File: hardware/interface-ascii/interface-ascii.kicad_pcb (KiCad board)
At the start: 2 copper layers, 88.9 x 119.4 mm, 47 parts, among them J1 Apple 1, J2 Apple 2, J3 Reset/Clr, J4 Keyboard, J5 ISP header, J6 UART, SW1 Options, U1 ATmega328P, U2 74LS138, U3 74LS166, U4 74LS138

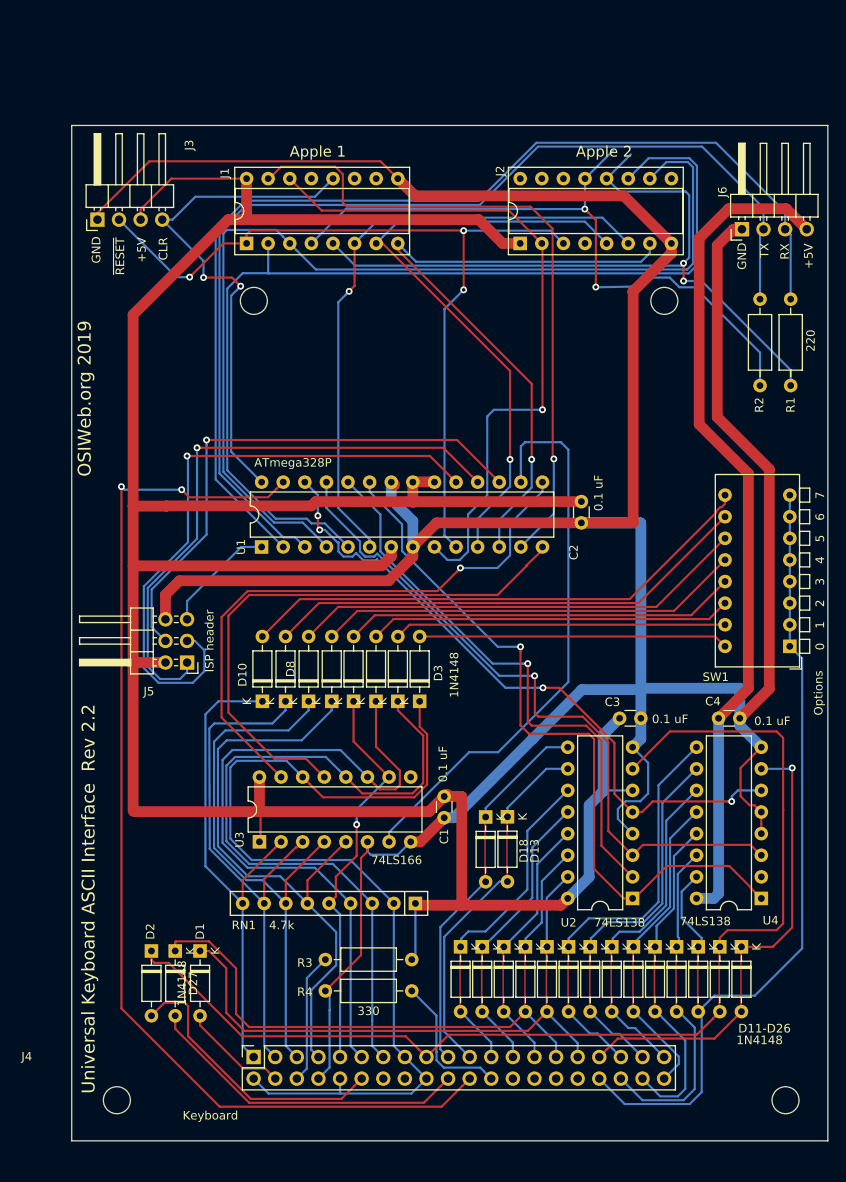
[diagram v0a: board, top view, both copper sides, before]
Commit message: OSI mounting holes
- Add OSI-compatible mounting holes.
- Adjust keyboard and aligner holes to make room for the OSI mounting holes
- Change "Universal Keyboard" to "Unified Keyboard" in the design files.
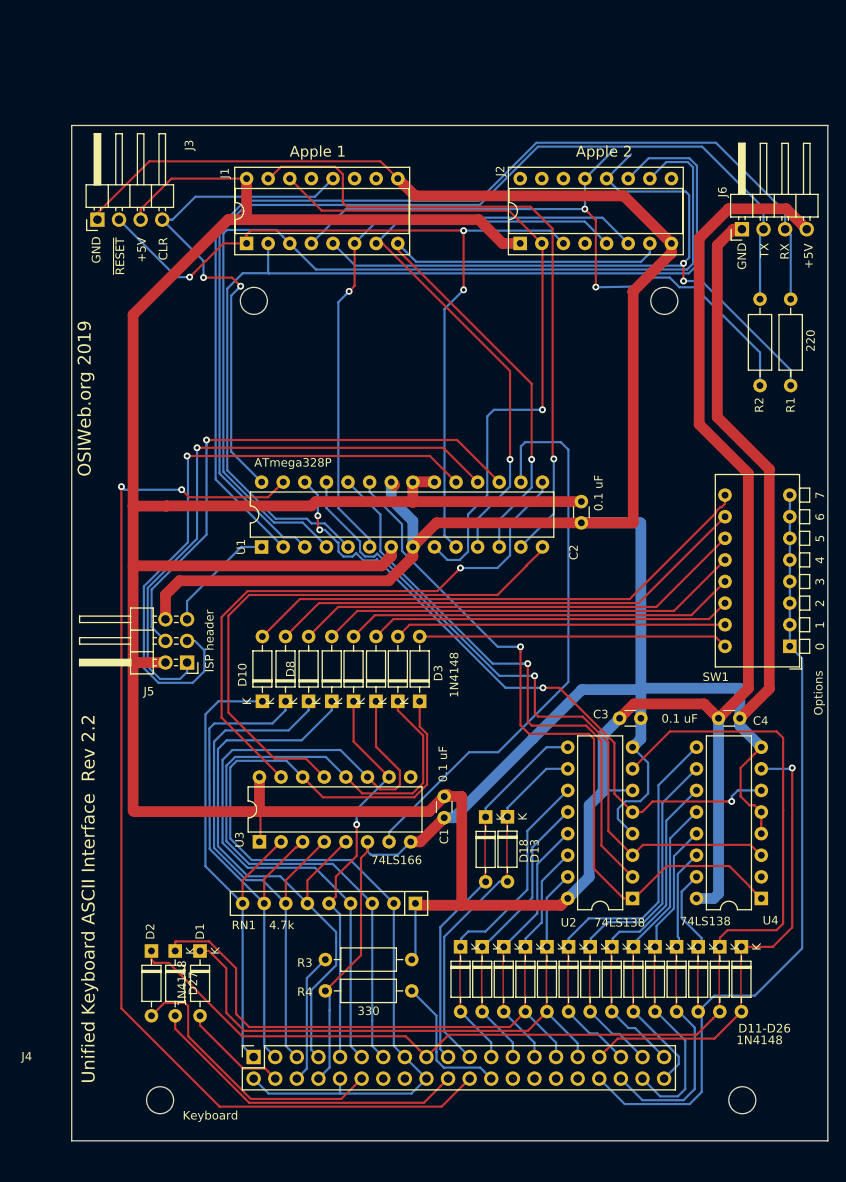
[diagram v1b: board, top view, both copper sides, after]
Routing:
- net +5V: track 436.8 -> 449.8 mm
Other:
- outline, holes or cut-outs redrawn
- board text added: "Unified Keyboard ASCII Interface Rev 2.2"
- board text removed: "Universal Keyboard ASCII Interface Rev 2.2"

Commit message: Keyboard interface cleanups for ASCII controller
Fixed lines for POWER LED and button, SHIFT Lock, Rubout, and CAPS LED.
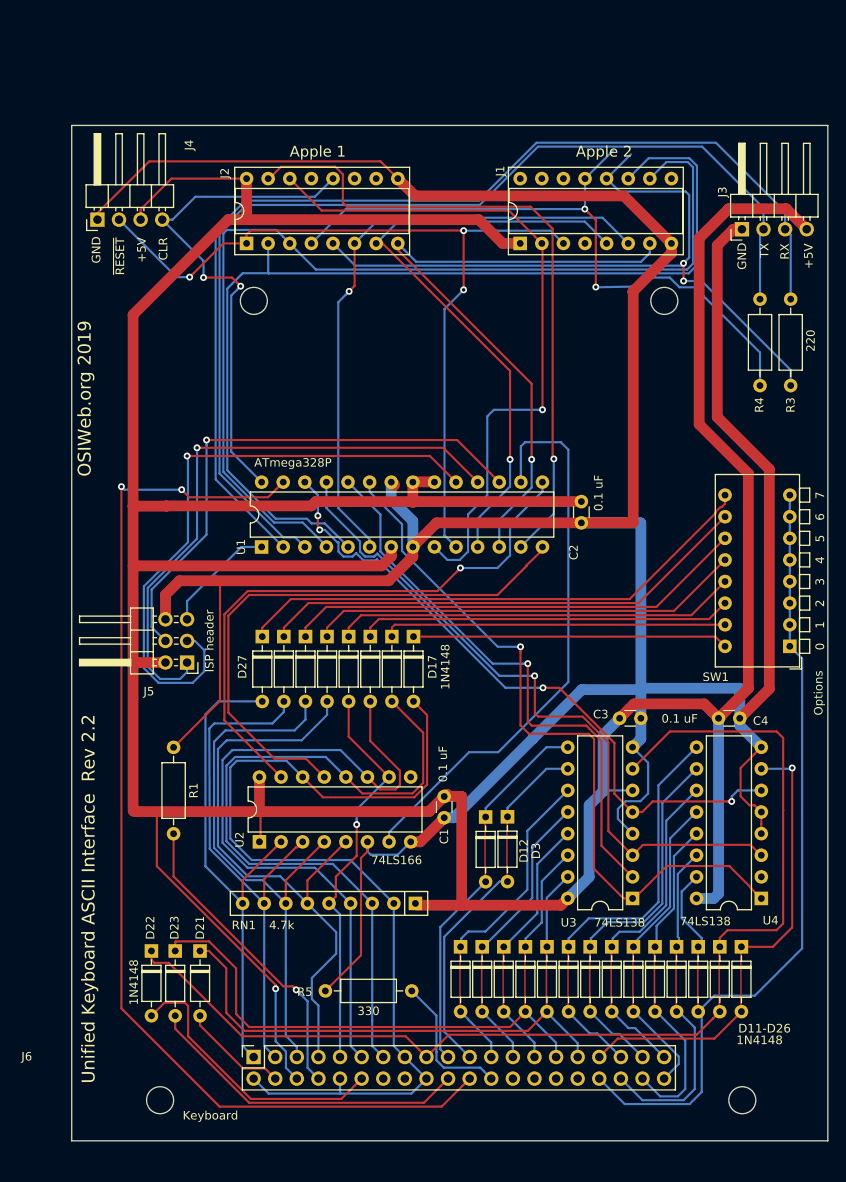
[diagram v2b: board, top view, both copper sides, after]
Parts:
- removed the D27 at (176.0, 160.6)
- removed the D3 at (204.7, 131.2)
- removed the D7 at (194.4, 131.2)
- removed the D8 at (191.7, 131.2)
- removed the R3 at (203.8, 161.6)
- added D17: 1N4148, Diode_THT:D_DO-35_SOD27_P7.62mm_Horizontal, F.Cu at (204.0, 123.6)
- added D19: 1N4148, Diode_THT:D_DO-35_SOD27_P7.62mm_Horizontal, F.Cu at (193.9, 123.6)
- added D23: 1N4148, Diode_THT:D_DO-35_SOD27_P7.62mm_Horizontal, F.Cu at (176.0, 160.6)
- added D26: 1N4148, Diode_THT:D_DO-35_SOD27_P7.62mm_Horizontal, F.Cu at (191.3, 123.6)
- added R1: 330, Resistor_THT:R_Axial_DIN0207_L6.3mm_D2.5mm_P10.16mm_Horizontal, F.Cu at (175.8, 136.6)
- moved D24 7.64 mm to (201.5, 123.6), turned to 270 degrees
- moved D18 7.64 mm to (198.9, 123.6), turned to 270 degrees
- moved D25 7.63 mm to (196.4, 123.6), turned to 270 degrees
- moved D20 7.61 mm to (188.8, 123.6), turned to 270 degrees
- moved D27 7.61 mm to (186.2, 123.6), turned to 270 degrees
- renumbered D11 to D1, D16 to D10, D17 to D11, D18 to D12, D23 to D13, D24 to D14, D25 to D15, D26 to D16, D5 to D18, D12 to D2, D9 to D20, D1 to D21, D2 to D22, D4 to D24, D6 to D25, D10 to D27, D13 to D3, D14 to D4, D19 to D5, D20 to D6, D21 to D7, D22 to D8, D15 to D9, J2 to J1, J1 to J2, J6 to J3, J3 to J4, J4 to J6, R1 to R3, R2 to R4, R4 to R5, U3 to U2, U2 to U3
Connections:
- D18 pad 1: /Col2 -> Net-(D18-Pad1)
- D18 pad 2: Net-(D5-Pad2) -> /Col2
- D20 pad 1: /Col6 -> Net-(D20-Pad1)
- D20 pad 2: Net-(D9-Pad2) -> /Col6
- D24 pad 1: /Col1 -> Net-(D24-Pad1)
- D24 pad 2: Net-(D4-Pad2) -> /Col1
- D25 pad 1: /Col3 -> Net-(D25-Pad1)
- D25 pad 2: Net-(D6-Pad2) -> /Col3
- D27 pad 1: /Col7 -> Net-(D27-Pad1)
- D27 pad 2: Net-(D10-Pad2) -> /Col7
- J6 pad 6: Net-(J4-Pad6) -> +5V
- J6 pad 8: GND -> Net-(J6-Pad8)
- SW1 pad 10: Net-(D9-Pad2) -> Net-(D20-Pad1)
- SW1 pad 13: Net-(D6-Pad2) -> Net-(D25-Pad1)
- SW1 pad 14: Net-(D5-Pad2) -> Net-(D18-Pad1)
- SW1 pad 15: Net-(D4-Pad2) -> Net-(D24-Pad1)
- SW1 pad 9: Net-(D10-Pad2) -> Net-(D27-Pad1)
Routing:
- net Net-(D27-Pad1): track 0.00 -> 62.6 mm
- net Net-(D10-Pad2): track 62.0 -> 0.00 mm
- net Net-(D20-Pad1): track 0.00 -> 58.3 mm
- net Net-(D9-Pad2): track 57.5 -> 0.00 mm
- net Net-(D25-Pad1): track 0.00 -> 47.5 mm
- net Net-(D6-Pad2): track 46.4 -> 0.00 mm
- net Net-(D18-Pad1): track 0.00 -> 44.0 mm
- net Net-(D5-Pad2): track 42.7 -> 0.00 mm
- net Net-(D24-Pad1): track 0.00 -> 40.4 mm
- net Net-(D4-Pad2): track 39.0 -> 0.00 mm
- net Net-(J6-Pad8): track 0.00 -> 36.5 mm, vias 0 -> 1
- net +5V: track 449.8 -> 481.3 mm, vias 0 -> 1
- net Net-(J4-Pad6): track 15.4 -> 0.00 mm
- net GND: track 396.4 -> 406.6 mm
- net Net-(D19-Pad1): track 50.0 -> 51.1 mm
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
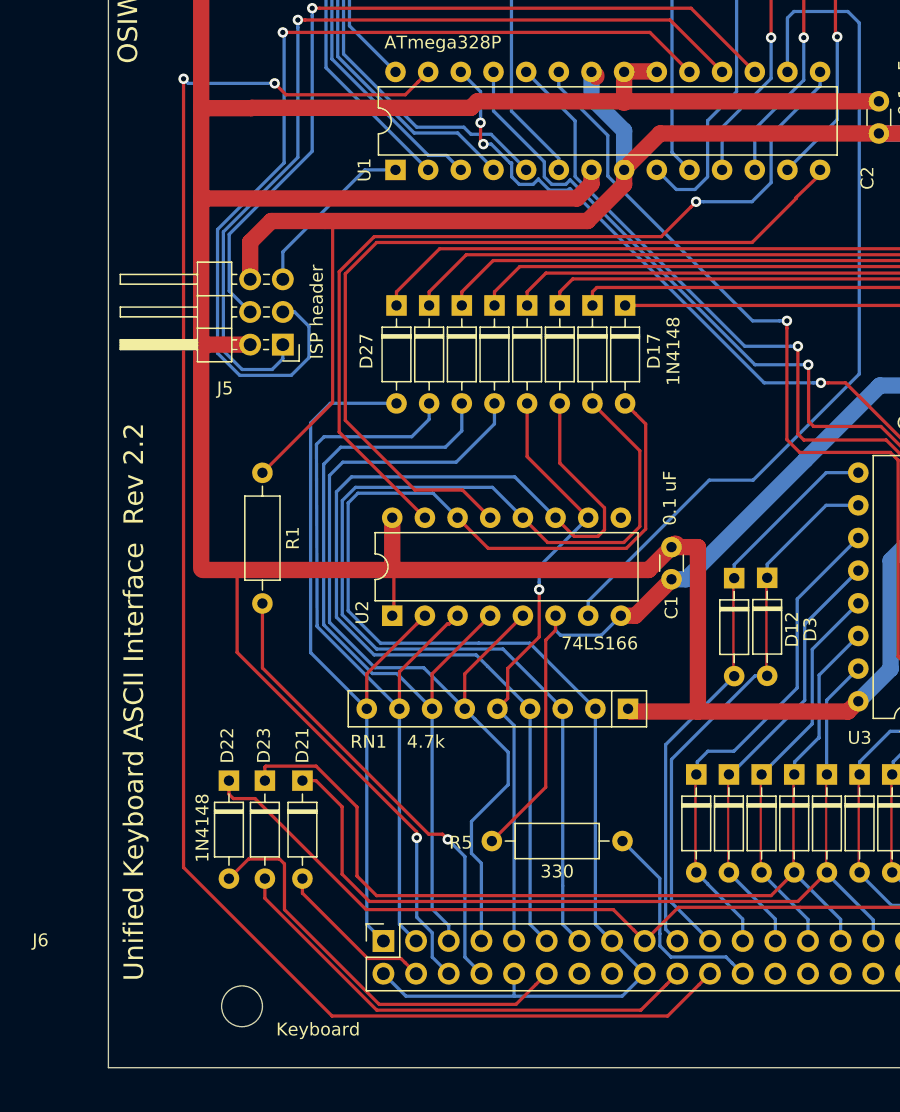
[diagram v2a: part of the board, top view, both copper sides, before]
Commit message: Finalize layout and mounting
- Add apple 2 mounting slots (and stretch PCB to accommodate slots
- Add pass-through holes in aligners for OSI keyboard spacers
- Move 'ESC' key next to '1' key
- Add TAB key next to Q key
- remove 'here is' and finalize "helper" keys along left side of keyboard
- move legends off of PCB traces
- update to release 1.3
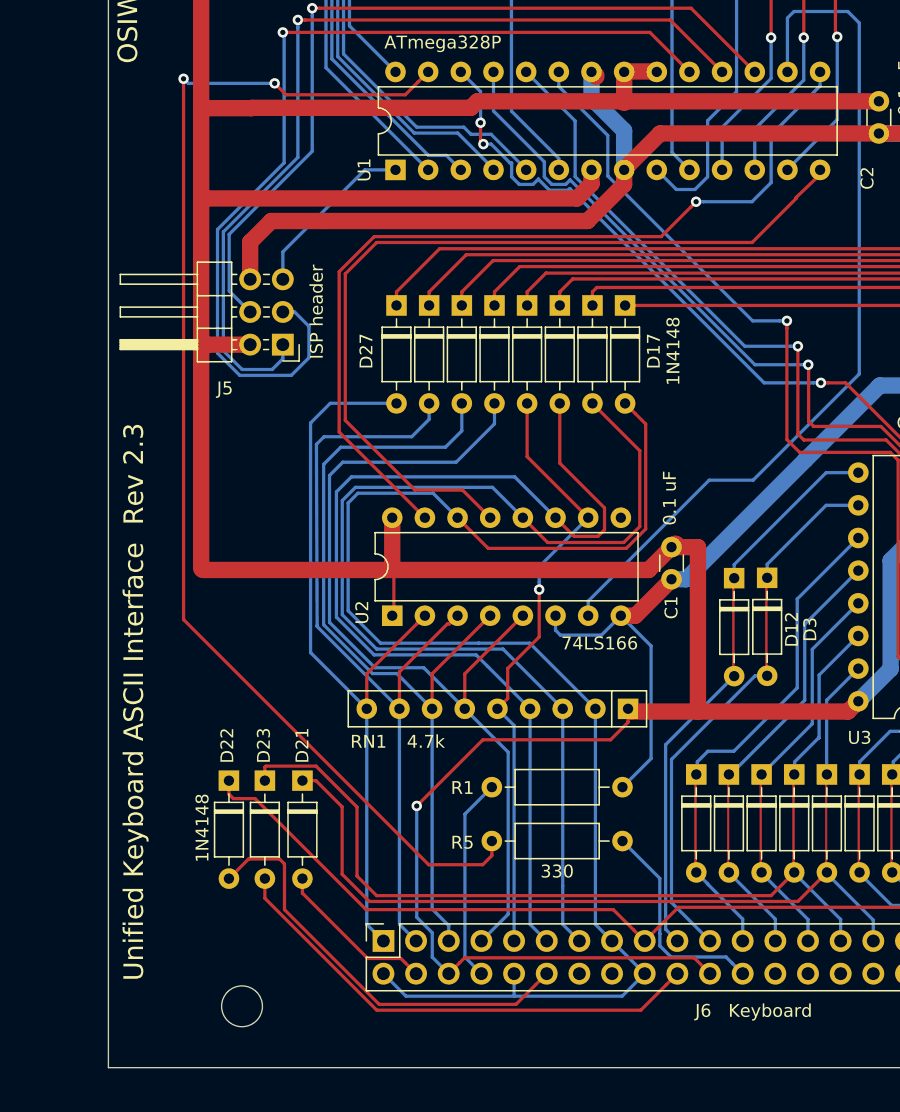
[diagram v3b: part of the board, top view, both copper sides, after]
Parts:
- moved R1 37.2 mm to (203.8, 161.1), turned to 180 degrees
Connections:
- J6 pad 22: /CAPS_LED -> +5V
- R5 pad 1: GND -> /CAPS_LED
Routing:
- net /CAPS_LED: track 128.7 -> 95.6 mm
- net GND: track 406.6 -> 381.0 mm
- net Net-(J6-Pad8): track 36.5 -> 15.9 mm, vias 1 -> 0
- net +5V: track 481.3 -> 498.8 mm
- net /Col4: track 70.9 -> 70.2 mm
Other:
- board text added: "Unified Keyboard ASCII Interface Rev 2.3"
- board text removed: "Unified Keyboard ASCII Interface Rev 2.2"

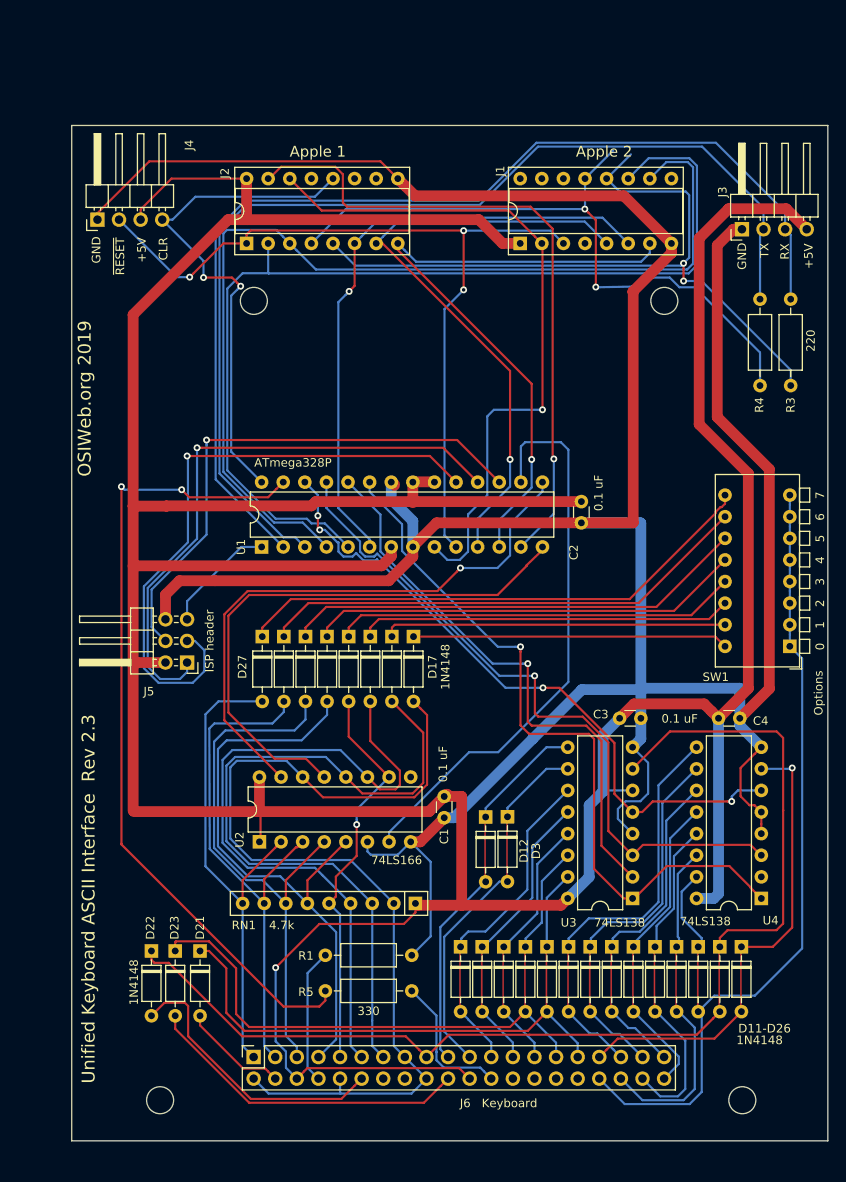
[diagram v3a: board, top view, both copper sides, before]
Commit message: ASCII interface update
- Fix wrong direction DIP switch diodes
- Add buffers to permit ISP lines to also be used as output and LED drivers
- Allow 3 keyboard LEDs and 3 host outputs (RESET, CLEAR, BREAK, LOCAL, etc.).
- Outputs 1 and 3 are general purpose (can be open drain or driven).  Output 2
  is open collector (with optional on-board pullup).
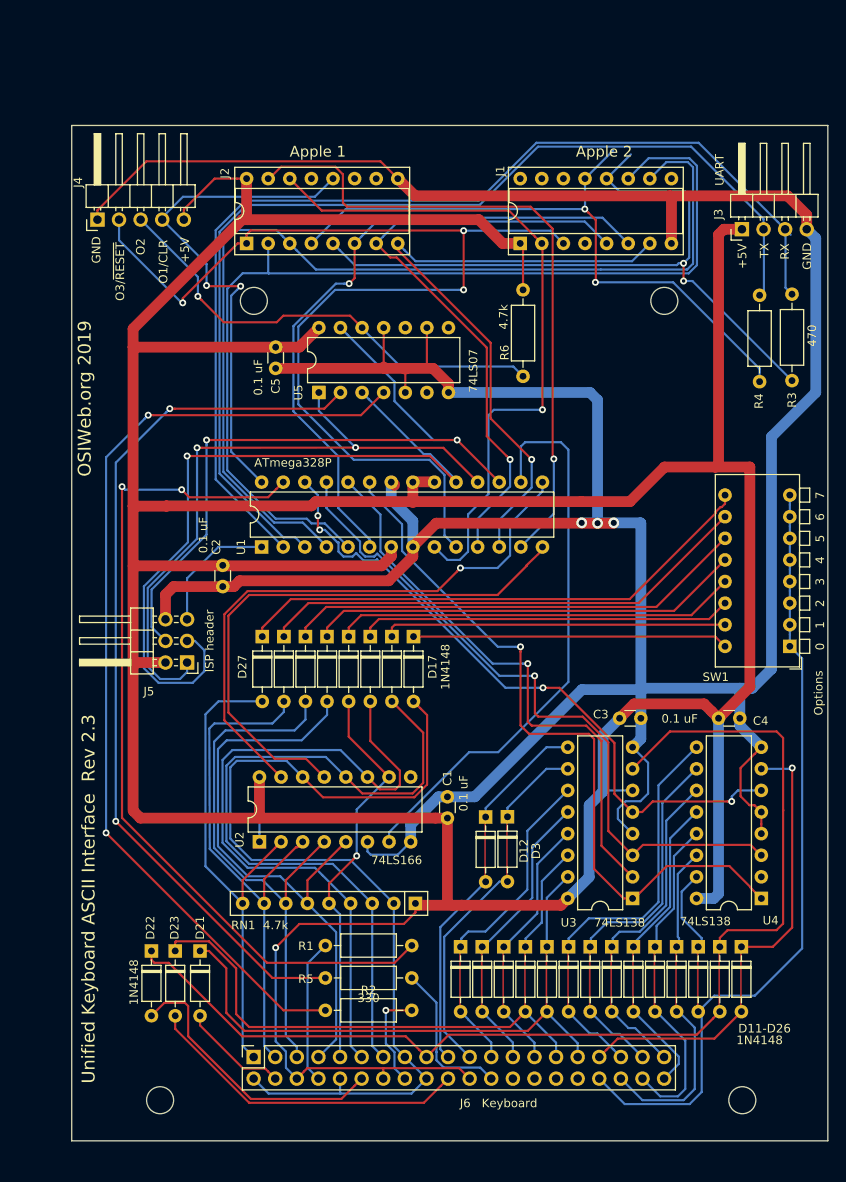
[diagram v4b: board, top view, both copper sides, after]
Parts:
- added C5: 0.1 uF, Capacitor_THT:C_Disc_D3.0mm_W1.6mm_P2.50mm, F.Cu at (187.8, 89.6)
- added R2: 330, Resistor_THT:R_Axial_DIN0207_L6.3mm_D2.5mm_P10.16mm_Horizontal, F.Cu at (193.7, 167.5)
- added R6: 4.7k, Resistor_THT:R_Axial_DIN0207_L6.3mm_D2.5mm_P10.16mm_Horizontal, F.Cu at (216.9, 82.8)
- added U5: 74LS07, Package_DIP:DIP-14_W7.62mm, F.Cu at (192.9, 94.9)
- J4: value Reset/Clr -> Conn_01x05; footprint Connector_PinHeader_2.54mm:PinHeader_1x04_P2.54mm_Horizontal -> Connector_PinHeader_2.54mm:PinHeader_1x05_P2.54mm_Horizontal
- R3: value 220 -> 470
- moved C2 42.8 mm to (181.6, 115.2)
- moved C1 2.57 mm to (208.0, 144.9), turned to 90 degrees
- moved R5 1.52 mm to (193.7, 163.7)
- moved R1 1.14 mm to (203.8, 159.9)
- moved R3 0.60 mm to (248.5, 93.5)
- moved R4 0.46 mm to (244.7, 93.6)
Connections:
- net /ClrScr renamed /OUT1
- net /MISO renamed /MISO-LED3
- net /MOSI renamed /MOSI-OUT2
- net /SCK renamed /SCK-LED2
- net /~SYS_RESET renamed /OUT3
- J3 pad 1: GND -> +5V
- J3 pad 4: +5V -> GND
- J4 pad 3: +5V -> /OUT2
- J6 pad 14: Net-(J6-Pad14) -> +5V
- R1 pad 1: GND -> /LED1
- R5 pad 1: /CAPS_LED -> Net-(R5-Pad1)
- U1 pad 27: /CAPS_LED -> /LED1
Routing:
- net Net-(R2-Pad1): track 0.00 -> 114.4 mm, vias 0 -> 2
- net Net-(R5-Pad1): track 0.00 -> 104.3 mm, vias 0 -> 2
- net /LED1: track 0.00 -> 101.1 mm, vias 0 -> 2
- net /CAPS_LED: track 95.6 -> 0.00 mm, vias 2 -> 0
- net /OUT2: track 0.00 -> 54.6 mm, vias 0 -> 1
- net GND: track 381.0 -> 414.7 mm, vias 0 -> 3
- net /OUT3: track 97.6 -> 130.1 mm
- net +5V: track 498.8 -> 528.6 mm
- net /MOSI-OUT2: track 63.4 -> 84.0 mm, vias 1 -> 2
- net /SCK-LED2: track 74.0 -> 89.6 mm
- net Net-(J6-Pad16): track 0.00 -> 12.0 mm, vias 0 -> 1
- net /MISO-LED3: track 69.5 -> 77.7 mm, vias 1 -> 2
- net /D4: track 72.6 -> 77.9 mm
- net /D1: track 79.1 -> 76.3 mm
- net /~RESET: track 13.5 -> 15.1 mm
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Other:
- board text added: "O1/CLR"
- board text added: "O2"
- board text added: "O3/~RESET"
- board text removed: "CLR"
- board text removed: "~RESET"
